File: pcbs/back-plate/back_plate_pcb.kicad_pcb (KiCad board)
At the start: 2 copper layers, 114.5 x 95.5 mm, 7 parts

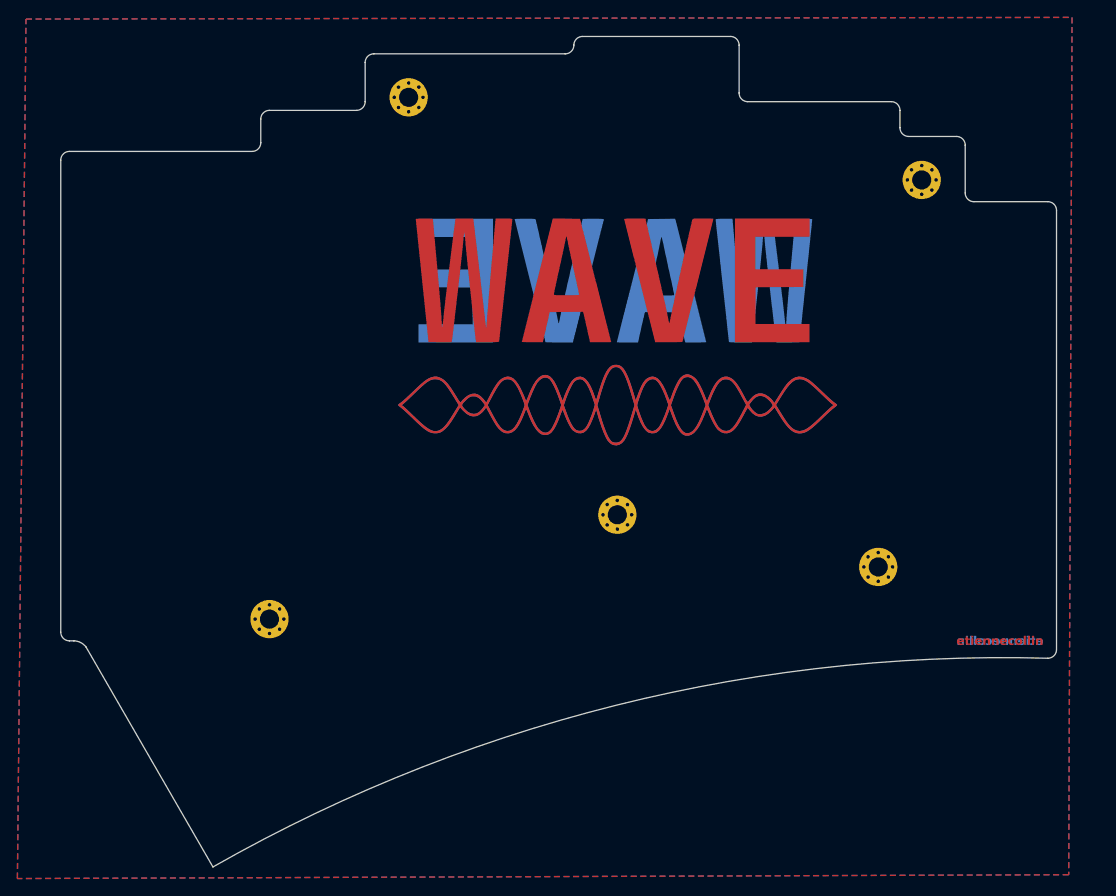
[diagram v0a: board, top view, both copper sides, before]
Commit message: Fixed spacing of PCB edges
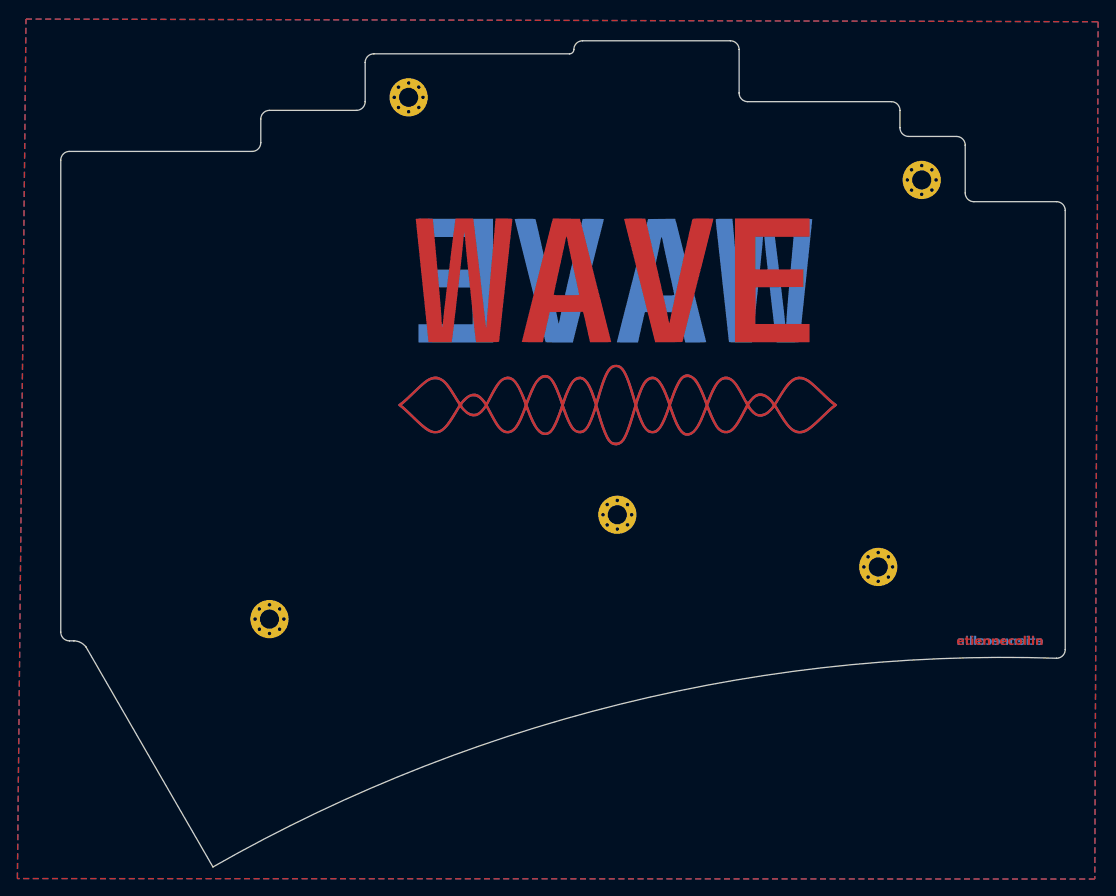
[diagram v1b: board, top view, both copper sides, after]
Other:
- board size 114.5 x 95.5 mm -> 115.5 x 95 mm
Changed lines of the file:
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@@
     (pad "1" thru_hole circle (at 1.65 0) (size 0.7 0.7) (drill 0.4) (layers "*.Cu" "*.Mask"))
   )
-  (gr_arc (start 144.5 41) (mid 145.207107 41.292893) (end 145.5 42)
+  (gr_arc (start 145.5 41) (mid 146.207107 41.292893) (end 146.5 42)
     (stroke (width 0.05) (type default)) (layer "Edge.Cuts"))
   (gr_line (start 32 35.22) (end 53 35.22)
     (stroke (width 0.05) (type default)) (layer "Edge.Cuts"))
-  (gr_line (start 91 22) (end 108 22)
+  (gr_line (start 91 22.5) (end 108 22.5)
     (stroke (width 0.05) (type default)) (layer "Edge.Cuts"))
-  (gr_line (start 136 41) (end 144.5 41)
+  (gr_line (start 136 41) (end 145.5 41)
     (stroke (width 0.05) (type default)) (layer "Edge.Cuts"))
-  (gr_line (start 67 24) (end 89 24)
+  (gr_arc (start 90 23.5) (mid 90.292893 22.792893) (end 91 22.5)
     (stroke (width 0.05) (type default)) (layer "Edge.Cuts"))
-  (gr_arc (start 48.5 117.5) (mid 94.852044 98.908178) (end 144.5 93.5)
+  (gr_line (start 67 24) (end 89.5 24)
+    (stroke (width 0.05) (type default)) (layer "Edge.Cuts"))
+  (gr_arc (start 48.5 117.5) (mid 95.337204 98.779534) (end 145.5 93.5)
     (stroke (width 0.05) (type default)) (layer "Edge.Cuts"))
   (gr_line (start 127.5 32.5) (end 127.5 30.5)
-    (stroke (width 0.05) (type default)) (layer "Edge.Cuts"))
-  (gr_arc (start 90 23) (mid 90.292893 22.292893) (end 91 22)
     (stroke (width 0.05) (type default)) (layer "Edge.Cuts"))
   (gr_arc (start 32 91.5) (mid 31.292893 91.207107) (end 31 90.5)
@@
   (gr_arc (start 66 25) (mid 66.292893 24.292893) (end 67 24)
     (stroke (width 0.05) (type default)) (layer "Edge.Cuts"))
-  (gr_line (start 145.5 42) (end 145.5 92.5)
+  (gr_line (start 146.5 42) (end 146.5 92.5)
     (stroke (width 0.05) (type default)) (layer "Edge.Cuts"))
   (gr_arc (start 128.5 33.5) (mid 127.792893 33.207107) (end 127.5 32.5)
@@
   (gr_line (start 54 31.5) (end 54 34.22)
     (stroke (width 0.05) (type default)) (layer "Edge.Cuts"))
-  (gr_arc (start 145.5 92.5) (mid 145.207107 93.207107) (end 144.5 93.5)
+  (gr_arc (start 146.5 92.5) (mid 146.207107 93.207107) (end 145.5 93.5)
     (stroke (width 0.05) (type default)) (layer "Edge.Cuts"))
   (gr_arc (start 110 29.5) (mid 109.292893 29.207107) (end 109 28.5)
@@
   (gr_arc (start 126.5 29.5) (mid 127.207107 29.792893) (end 127.5 30.5)
     (stroke (width 0.05) (type default)) (layer "Edge.Cuts"))
-  (gr_line (start 109 23) (end 109 28.5)
+  (gr_line (start 109 23.5) (end 109 28.5)
     (stroke (width 0.05) (type default)) (layer "Edge.Cuts"))
   (gr_arc (start 32.5 91.5) (mid 33.279998 91.690003) (end 33.9 92.2)
@@
   (gr_line (start 31 90.5) (end 31 36.22)
     (stroke (width 0.05) (type default)) (layer "Edge.Cuts"))
-  (gr_arc (start 108 22) (mid 108.707107 22.292893) (end 109 23)
+  (gr_arc (start 108 22.5) (mid 108.707107 22.792893) (end 109 23.5)
     (stroke (width 0.05) (type default)) (layer "Edge.Cuts"))
   (gr_arc (start 54 31.5) (mid 54.292893 30.792893) (end 55 30.5)
@@
   (gr_arc (start 54 34.22) (mid 53.707107 34.927107) (end 53 35.22)
     (stroke (width 0.05) (type default)) (layer "Edge.Cuts"))
+  (gr_arc (start 90 23.5) (mid 89.853553 23.853553) (end 89.5 24)
+    (stroke (width 0.05) (type default)) (layer "Edge.Cuts"))
   (gr_arc (start 31 36.22) (mid 31.292893 35.512893) (end 32 35.22)
     (stroke (width 0.05) (type default)) (layer "Edge.Cuts"))
@@
     (stroke (width 0.05) (type default)) (layer "Edge.Cuts"))
   (gr_line (start 110 29.5) (end 126.5 29.5)
-    (stroke (width 0.05) (type default)) (layer "Edge.Cuts"))
-  (gr_arc (start 90 23) (mid 89.707107 23.707107) (end 89 24)
     (stroke (width 0.05) (type default)) (layer "Edge.Cuts"))
   (zone (net 0) (net_name "") (layers "F&B.Cu") (name "Ground") (hatch edge 0.508)
@@
     (polygon
       (pts
-        (xy 147.285298 19.809186)
-        (xy 146.901563 118.389311)
+        (xy 150.285298 20.309186)
+        (xy 149.901563 118.889311)
         (xy 26.012915 118.834236)
         (xy 27 20)
